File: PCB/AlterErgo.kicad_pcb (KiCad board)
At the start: 2 copper layers, 170.4 x 144.9 mm, 105 parts, among them J1 GS3, J2 SJ-43514, J3 GS3, SW0:10 SW_Push, SW0:11 SW_Push, SW0:12 SW_Push, SW0:7 SW_Push, SW0:8 SW_Push, SW0:9 SW_Push, SW1 SW_SPST, SW1:10 SW_Push, SW1:11 SW_Push, SW1:12 SW_Push, SW1:13 SW_Push, SW1:7 SW_Push, SW1:8 SW_Push, SW1:9 SW_Push, SW2:10 SW_Push, SW2:11 SW_Push, SW2:12 SW_Push, SW2:13 SW_Push, SW2:7 SW_Push, SW2:8 SW_Push, SW2:9 SW_Push, SW3:10 SW_Push, SW3:11 SW_Push, SW3:12 SW_Push, SW3:13 SW_Push, SW3:8 SW_Push, SW3:9 SW_Push, SW4:10 SW_Push, SW4:11 SW_Push, SW4:12 SW_Push, SW4:13 SW_Push, SW4:7 SW_Push, SW4:8 SW_Push, SW4:9 SW_Push, SW5:10 SW_Push, SW5:11 SW_Push, SW5:12 SW_Push, SW5:13 SW_Push, SW5:7 SW_Push, SW5:8 SW_Push, SW5:9 SW_Push, U1 Feather32u4Bluefruit, U2 MCP23018

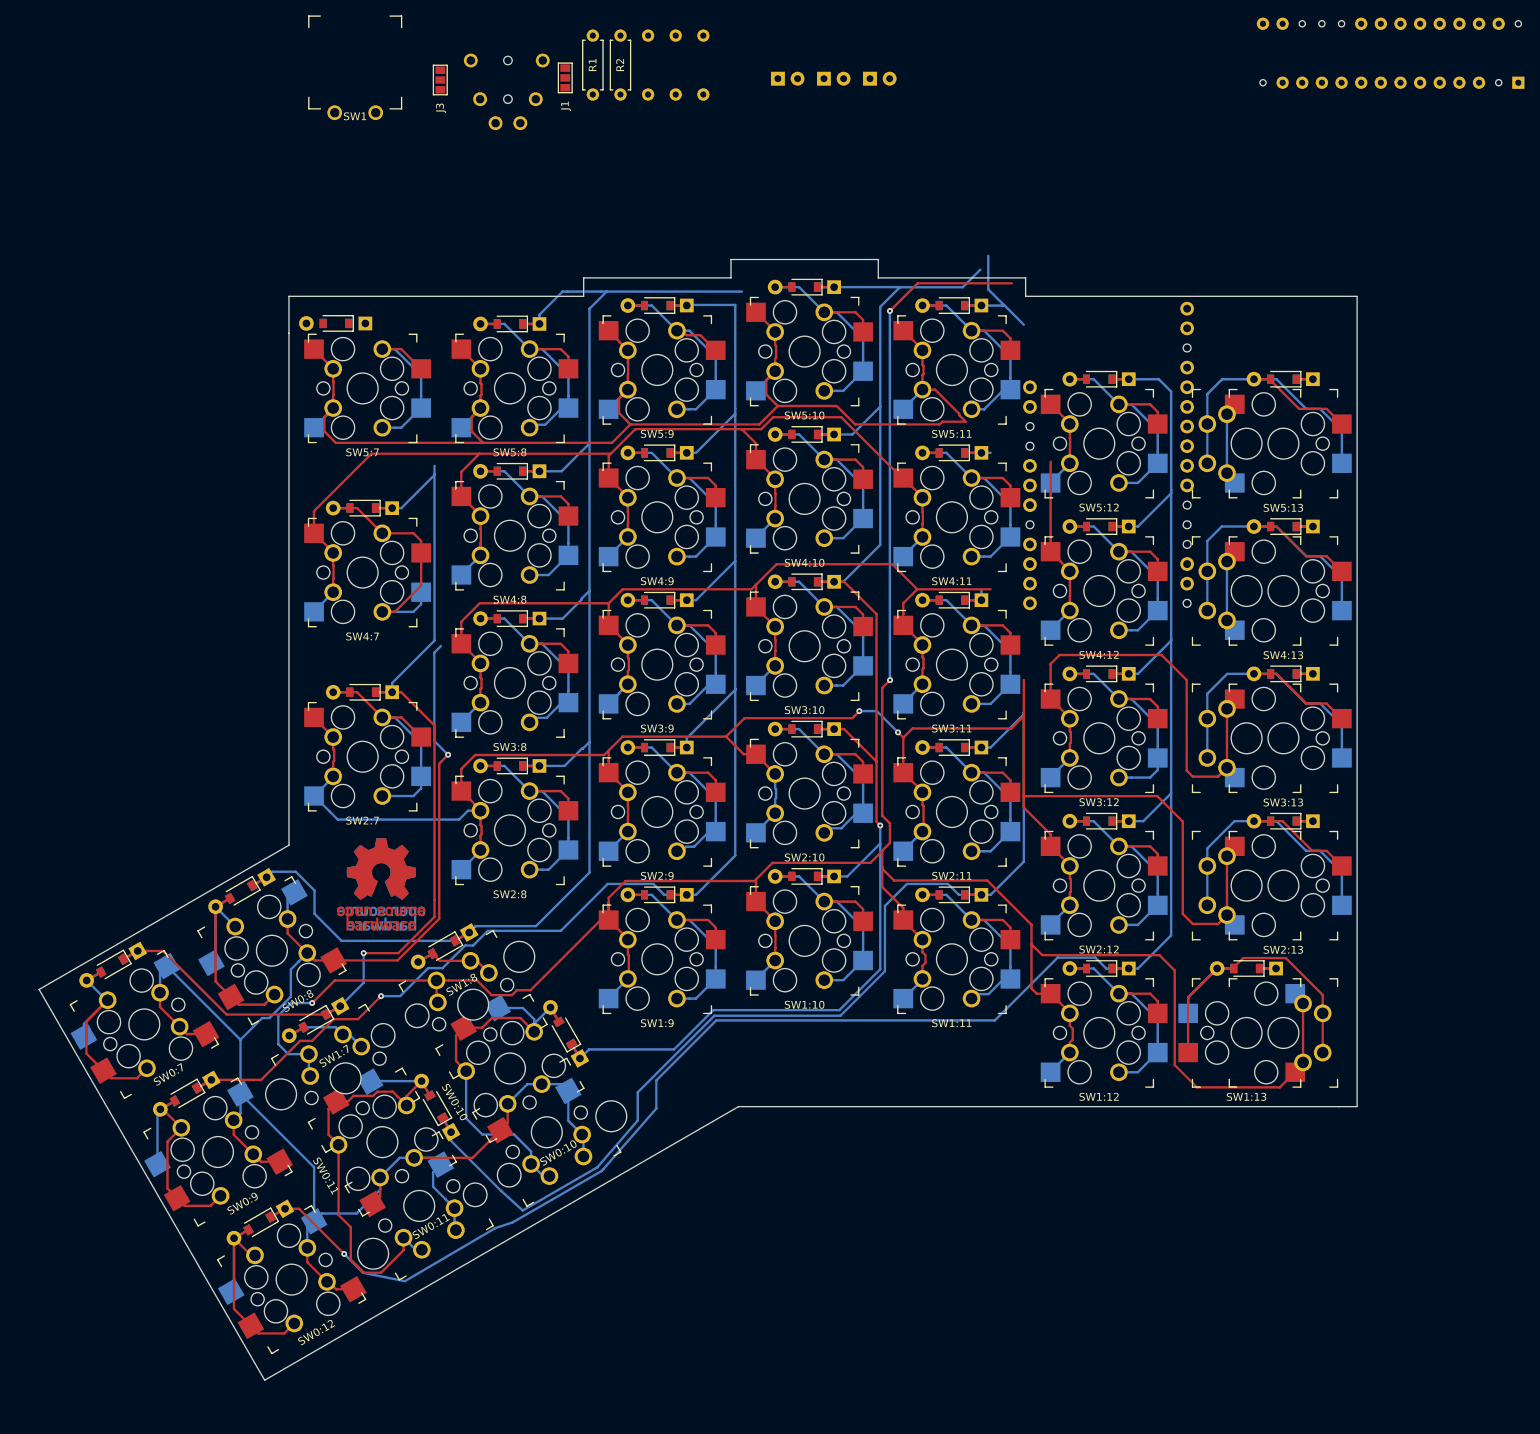
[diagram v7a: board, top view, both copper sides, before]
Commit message: Route traces for Feather and breakout board in new positions
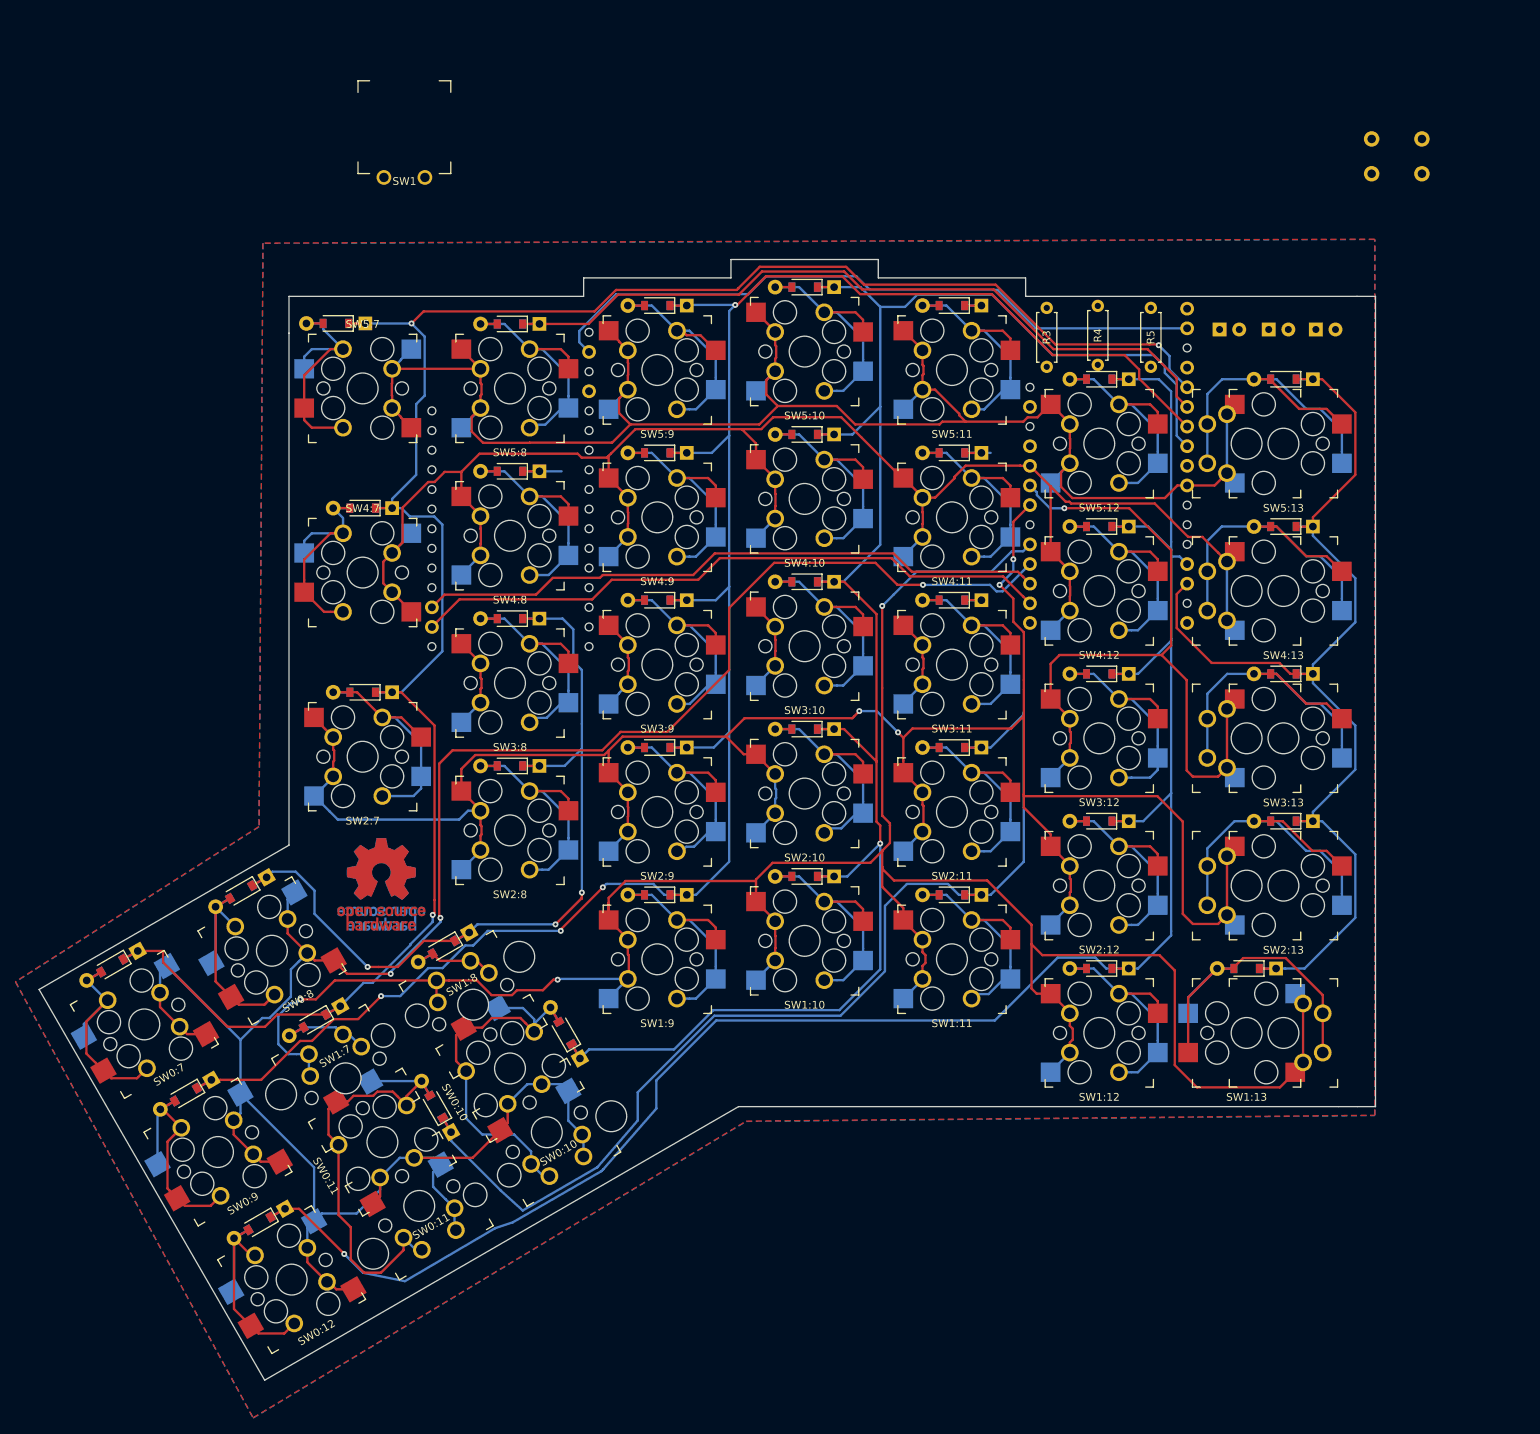
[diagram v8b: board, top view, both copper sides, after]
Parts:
- removed J1, J3: GS3, Connectors:GS3
- removed J2: SJ-43514, keyboard_accessories:TRRS_Jack_SJ-43514_reversible
- removed R1, R2: 2.2k, Resistors_THT:R_Axial_DIN0207_L6.3mm_D2.5mm_P7.62mm_Horizontal
- added SW2: SW_Push, Buttons_Switches_THT:SW_PUSH_6mm, B.Cu at (217.9, 24.9)
- R3, R4, R5: moved to F.Cu
- U1: value Feather32u4Bluefruit -> FeatherBreakout; footprint keyboard_accessories:Feather32u4Bluefruit -> IOBreakout:FeatherBreakout
- U2: value MCP23018 -> FeatherBreakout; footprint Housings_DIP:DIP-28_W7.62mm -> IOBreakout:FeatherBreakout
- moved U2 140.1 mm to (100.1, 68.9), turned to 270 degrees
- moved R5 70.6 mm to (182.9, 46.7), turned to 270 degrees
- moved D1 66.1 mm to (204.2, 49.5)
- moved D2 66.0 mm to (198.1, 49.5)
- moved D3 65.7 mm to (191.8, 49.5)
- moved R4 61.0 mm to (176.0, 46.5), turned to 270 degrees
- moved R3 52.3 mm to (169.4, 46.7), turned to 270 degrees
- moved SW1 10.5 mm to (86.4, 23.4)
- turned SW4:7 to 180 degrees
- turned SW5:7 to 180 degrees
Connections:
- net Net-(SW1-Pad2) renamed /ENABLE
- R3 pad 2: Net-(R3-Pad2) -> /LED1
- R4 pad 2: Net-(R4-Pad2) -> /LED2
- R5 pad 2: Net-(R5-Pad2) -> /LED3
- U1 pad 28: (no net) -> /RESET
- U2 pad 11: +3V3 -> /SCL
- U2 pad 12: /SCL -> /SDA
- U2 pad 25: /COL5 -> GND
- U2 pad 27: Net-(R5-Pad2) -> +3V3
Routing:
- net /COL6: track 135.3 -> 276.6 mm, vias 1 -> 3
- net /COL0: track 21.9 -> 146.0 mm
- net +3V3: track 0.00 -> 87.6 mm
- net /SDA: track 0.00 -> 83.4 mm
- net /SCL: track 0.00 -> 81.8 mm
- net /ROW0: track 231.2 -> 311.3 mm, vias 1 -> 3
- net /COL4: track 209.6 -> 270.5 mm, vias 1 -> 4
- net /ROW3: track 201.1 -> 150.2 mm, vias 0 -> 1
- net /COL10: track 207.6 -> 243.9 mm
- net /ROW1: track 351.0 -> 316.4 mm
- net /ROW4: track 198.2 -> 230.8 mm
- net /ROW5: track 199.0 -> 224.6 mm
- net /ROW2: track 265.5 -> 291.0 mm, vias 2 -> 4
- net /COL5: track 203.7 -> 220.3 mm, vias 0 -> 3
- net /COL11: track 172.5 -> 157.5 mm
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- added copper zone on B.Cu, net GND
- added copper zone on F.Cu, net GND
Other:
- board size 170.4 x 144.9 mm -> 172.8 x 144.9 mm
